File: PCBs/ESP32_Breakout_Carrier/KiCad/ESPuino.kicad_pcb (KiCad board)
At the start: 2 copper layers, 72.4 x 82.6 mm, 17 parts, among them J1 SD-Card Reader, J2 RFID-RC522, J3 Adafruit MAX98357, J4 Rotary Encode, J5 Next, J6 Prev, J7 Pause, J8 WS2812, J9 Power, Q1 BC337, Q2 IRF9540N, U1 ESP32-DEVKITC-32U

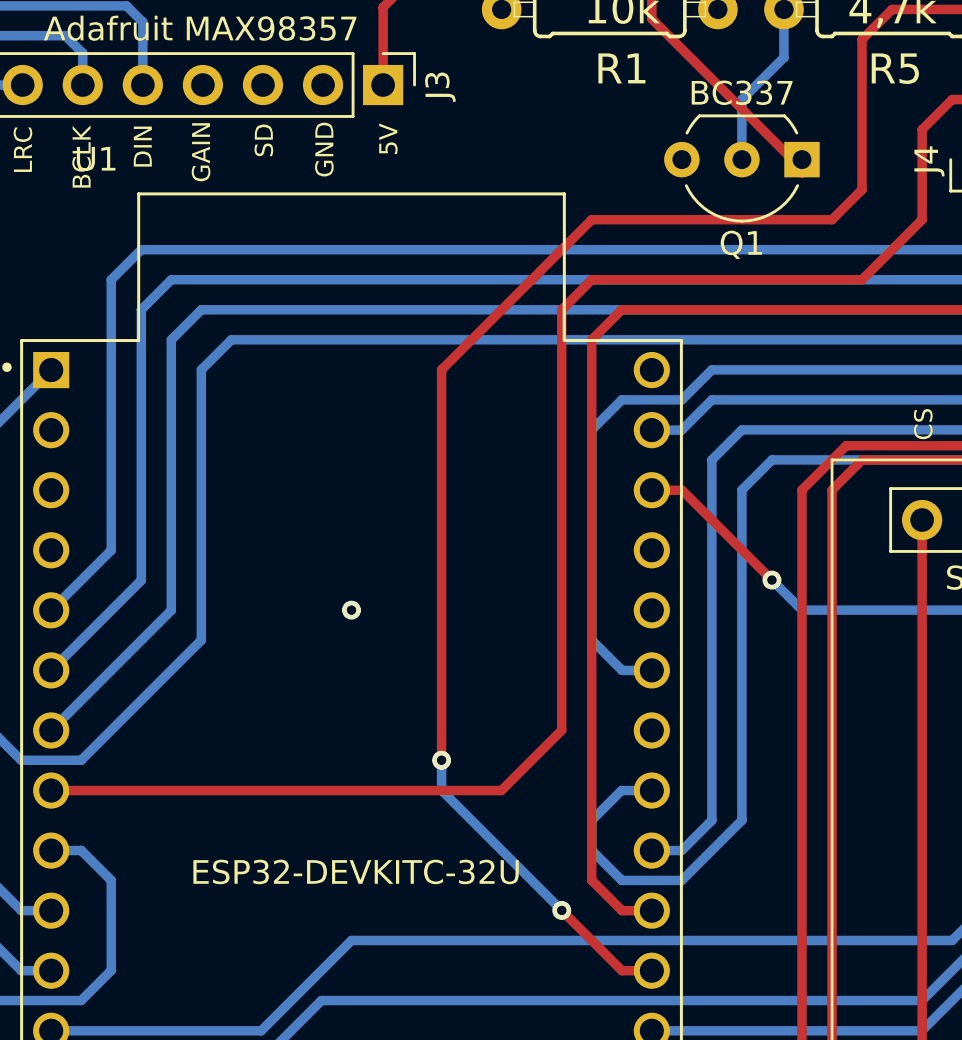
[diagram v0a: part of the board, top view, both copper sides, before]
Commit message: use snapEDA footprint and create 3d-model for ESP32_Breakout_Carrier
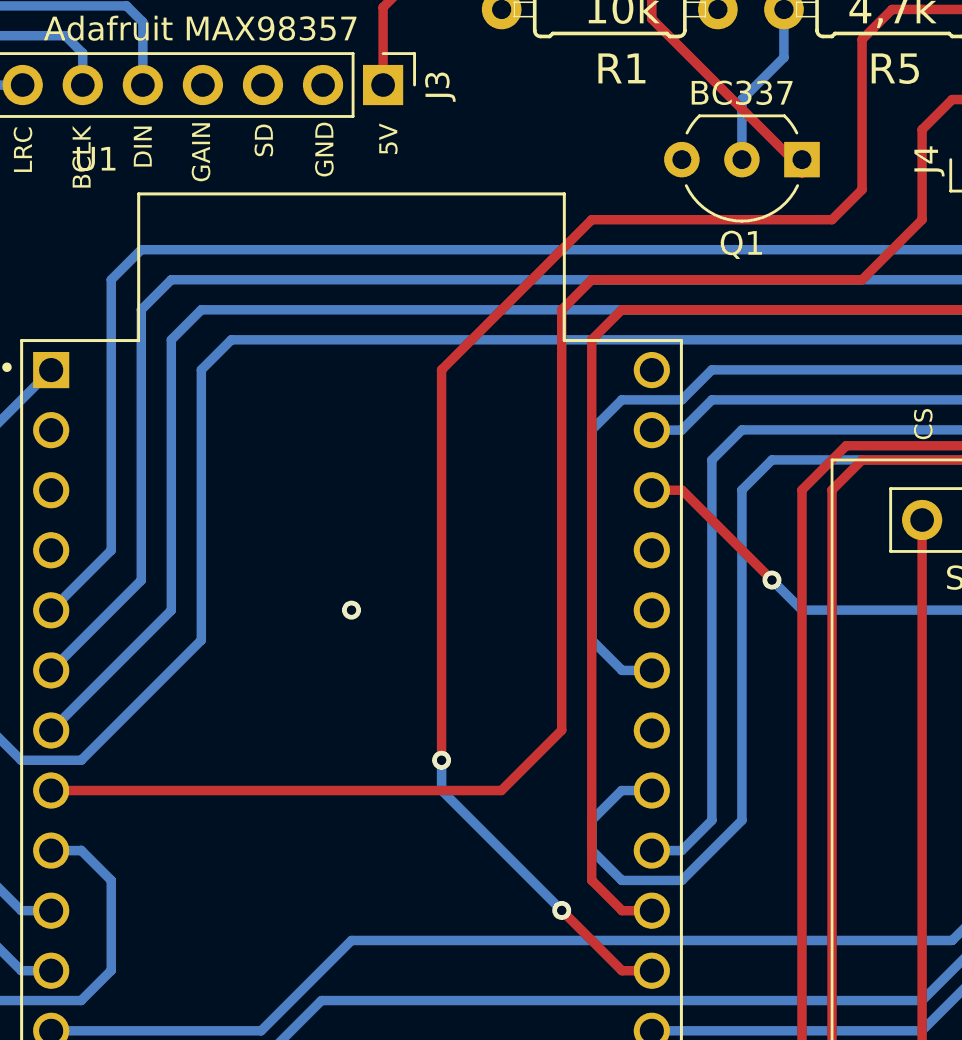
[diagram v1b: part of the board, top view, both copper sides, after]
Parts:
- U1: footprint ESP32-DEVKITC-32U:MODULE_ESP32-DEVKITC-32U -> ESPuino_snapEDA:MODULE_ESP32-DEVKITC-32U
